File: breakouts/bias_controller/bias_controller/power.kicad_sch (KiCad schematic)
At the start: 47 parts, among them U17 ADM7172, U18 LT3094xMSE, U21 TPS63070RNMT, U22 ADM7172, U23 ADM7172, U7 LM2776

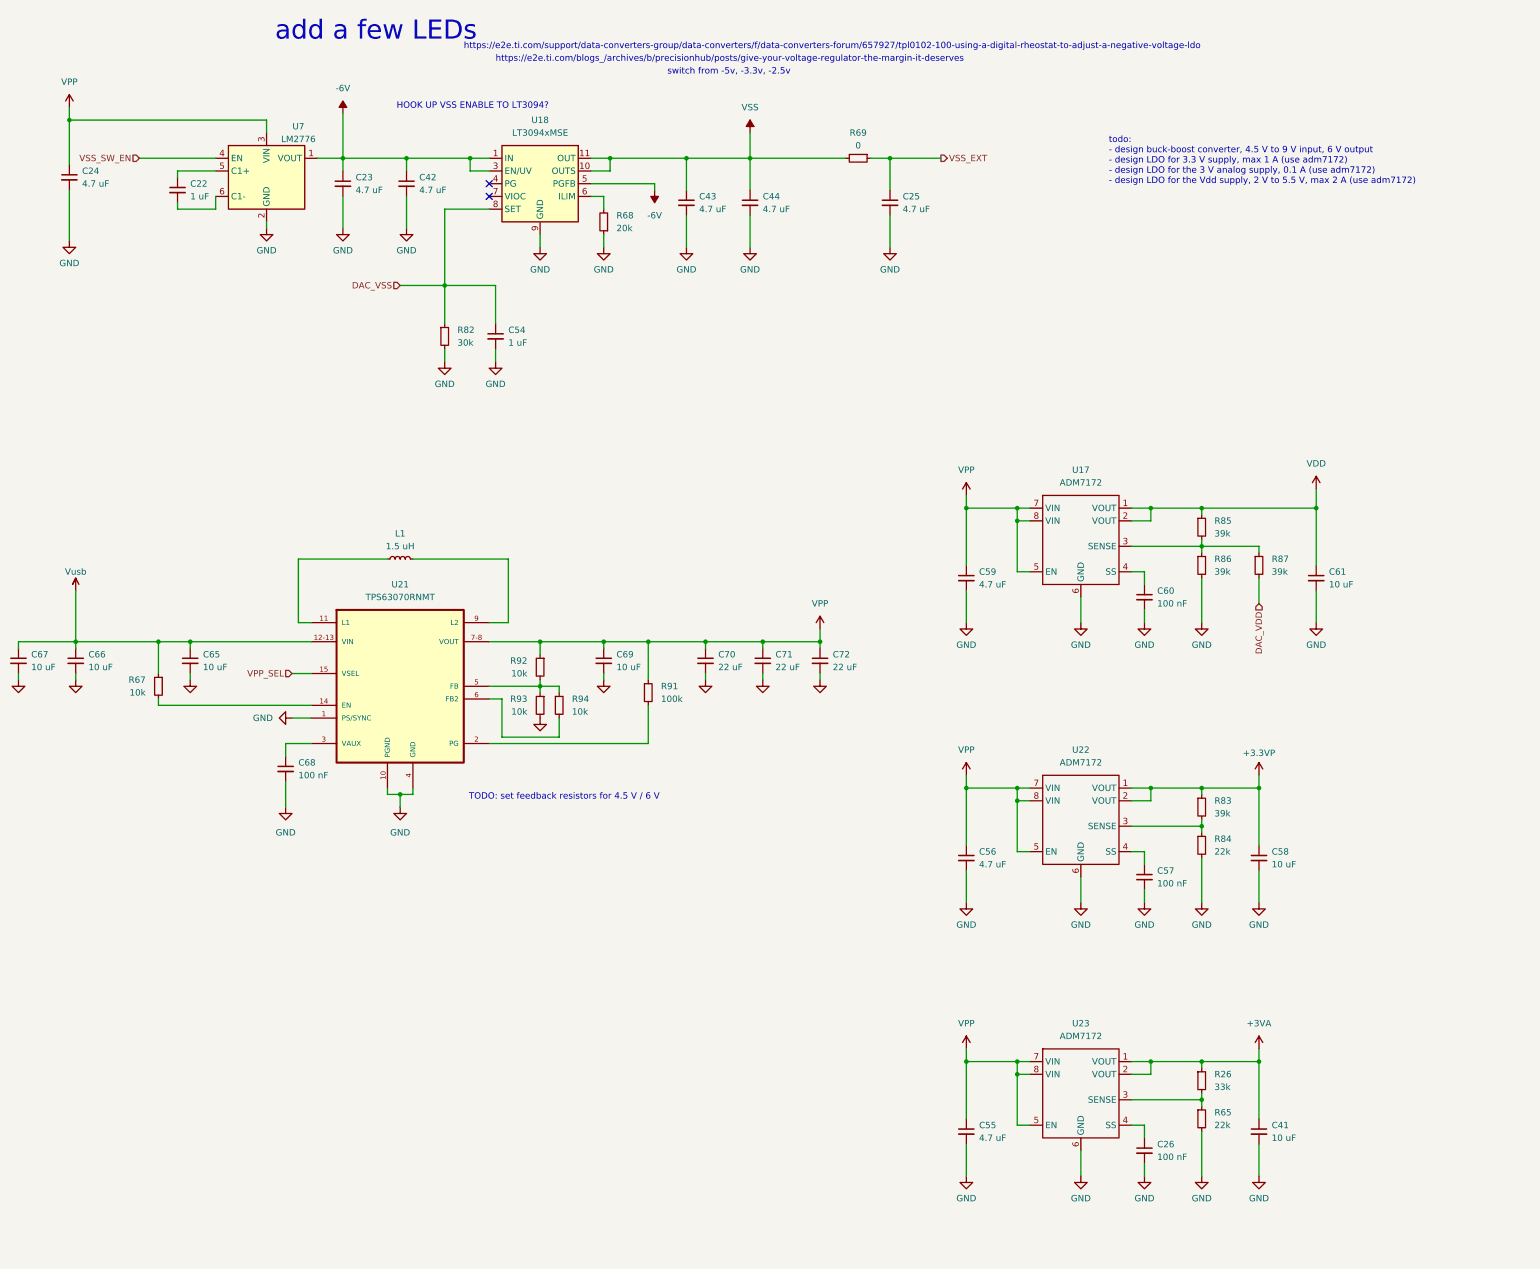
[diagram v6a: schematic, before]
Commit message: most footprint assignments on bias controller board, schematic cleanup
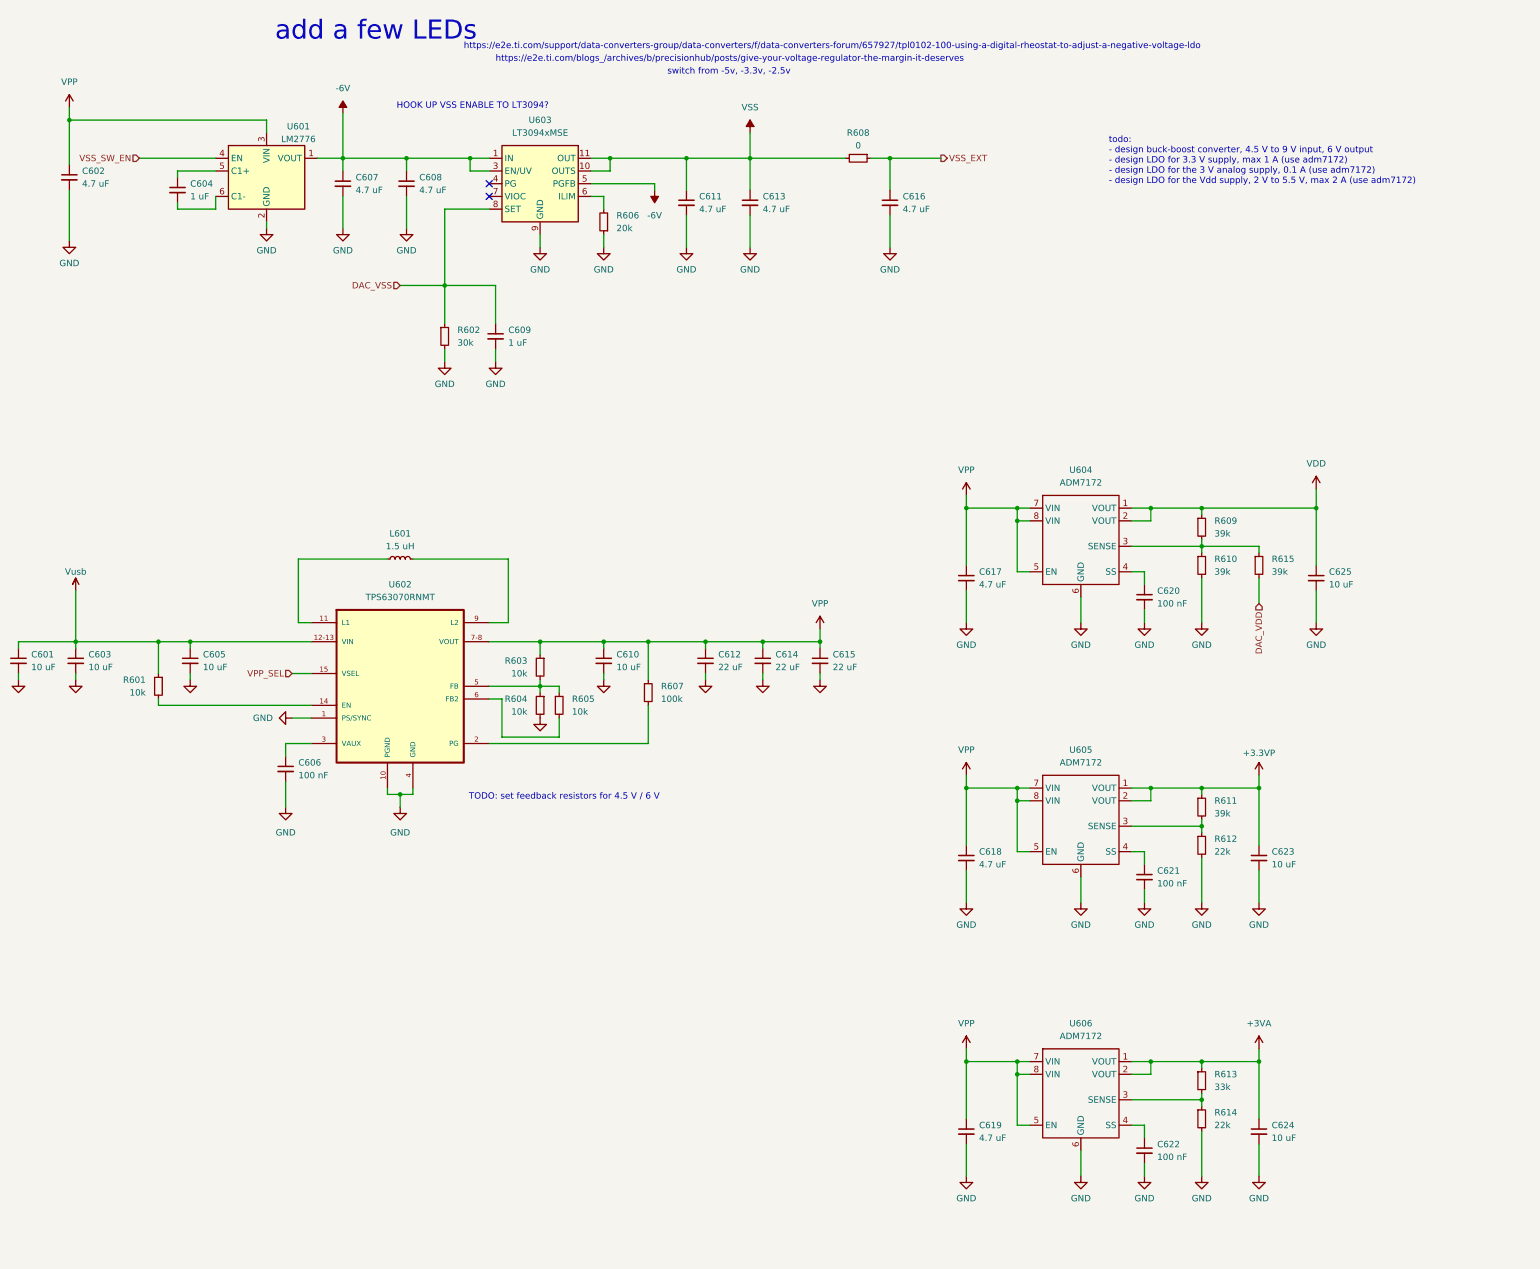
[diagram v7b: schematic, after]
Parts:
- C601: renamed from C67; footprint (none) -> Capacitor_SMD:C_0603_1608Metric
- C602: renamed from C24; footprint (none) -> Capacitor_SMD:C_0603_1608Metric
- C603: renamed from C66; footprint (none) -> Capacitor_SMD:C_0603_1608Metric
- C604: renamed from C22; footprint (none) -> Capacitor_SMD:C_0402_1005Metric
- C605: renamed from C65; footprint (none) -> Capacitor_SMD:C_0603_1608Metric
- C606: renamed from C68; footprint (none) -> Capacitor_SMD:C_0402_1005Metric
- C607: renamed from C23; footprint (none) -> Capacitor_SMD:C_0603_1608Metric
- C608: renamed from C42; footprint (none) -> Capacitor_SMD:C_0603_1608Metric
- C609: renamed from C54; footprint (none) -> Capacitor_SMD:C_0402_1005Metric
- C610: renamed from C69; footprint (none) -> Capacitor_SMD:C_0603_1608Metric
- C611: renamed from C43; footprint (none) -> Capacitor_SMD:C_0603_1608Metric
- C612: renamed from C70; footprint (none) -> Capacitor_SMD:C_0805_2012Metric
- C613: renamed from C44; footprint (none) -> Capacitor_SMD:C_0603_1608Metric
- C614: renamed from C71; footprint (none) -> Capacitor_SMD:C_0805_2012Metric
- C615: renamed from C72; footprint (none) -> Capacitor_SMD:C_0805_2012Metric
- C616: renamed from C25; footprint (none) -> Capacitor_SMD:C_0603_1608Metric
- C617: renamed from C59; footprint (none) -> Capacitor_SMD:C_0603_1608Metric
- C618: renamed from C56; footprint (none) -> Capacitor_SMD:C_0603_1608Metric
- C619: renamed from C55; footprint (none) -> Capacitor_SMD:C_0603_1608Metric
- C620: renamed from C60; footprint (none) -> Capacitor_SMD:C_0402_1005Metric
- C621: renamed from C57; footprint (none) -> Capacitor_SMD:C_0402_1005Metric
- C622: renamed from C26; footprint (none) -> Capacitor_SMD:C_0402_1005Metric
- C623: renamed from C58; footprint (none) -> Capacitor_SMD:C_0603_1608Metric
- C624: renamed from C41; footprint (none) -> Capacitor_SMD:C_0603_1608Metric
- C625: renamed from C61; footprint (none) -> Capacitor_SMD:C_0603_1608Metric
- L601: renamed from L1; footprint (none) -> Inductor_SMD:L_Coilcraft_XxL4020
- R601: renamed from R67; footprint (none) -> Resistor_SMD:R_0402_1005Metric
- R602: renamed from R82; footprint (none) -> Resistor_SMD:R_0402_1005Metric
- R603: renamed from R92; footprint (none) -> Resistor_SMD:R_0402_1005Metric
- R604: renamed from R93; footprint (none) -> Resistor_SMD:R_0402_1005Metric
- R605: renamed from R94; footprint (none) -> Resistor_SMD:R_0402_1005Metric
- R606: renamed from R68; footprint (none) -> Resistor_SMD:R_0402_1005Metric
- R607: renamed from R91; footprint (none) -> Resistor_SMD:R_0402_1005Metric
- R608: renamed from R69; footprint (none) -> Resistor_SMD:R_0402_1005Metric
- R609: renamed from R85; footprint (none) -> Resistor_SMD:R_0402_1005Metric
- R610: renamed from R86; footprint (none) -> Resistor_SMD:R_0402_1005Metric
- R611: renamed from R83; footprint (none) -> Resistor_SMD:R_0402_1005Metric
- R612: renamed from R84; footprint (none) -> Resistor_SMD:R_0402_1005Metric
- R613: renamed from R26; footprint (none) -> Resistor_SMD:R_0402_1005Metric
- R614: renamed from R65; footprint (none) -> Resistor_SMD:R_0402_1005Metric
- R615: renamed from R87; footprint (none) -> Resistor_SMD:R_0402_1005Metric
- renumbered U7 to U601, U21 to U602, U18 to U603, U17 to U604, U22 to U605, U23 to U606
